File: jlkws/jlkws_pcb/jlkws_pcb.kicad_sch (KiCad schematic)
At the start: 38 parts, among them J0 Conn_01x02_Socket, SW0 SWITCH, SW1 SWITCH, SW10 SWITCH, SW11 SWITCH, SW12 SWITCH, SW13 SWITCH, SW14 SWITCH, SW15 SWITCH, SW16 SWITCH, SW17 SWITCH, SW18 SWITCH, SW19 SWITCH, SW2 SWITCH, SW20 SWITCH, SW21 SWITCH, SW22 SWITCH, SW23 SWITCH, SW24 SWITCH, SW25 SWITCH, SW26 SWITCH, SW27 SWITCH, SW28 SWITCH, SW29 SWITCH, SW3 SWITCH, SW4 SWITCH, SW5 SWITCH, SW6 SWITCH, SW7 SWITCH, SW8 SWITCH, SW9 SWITCH, U0 NICE!

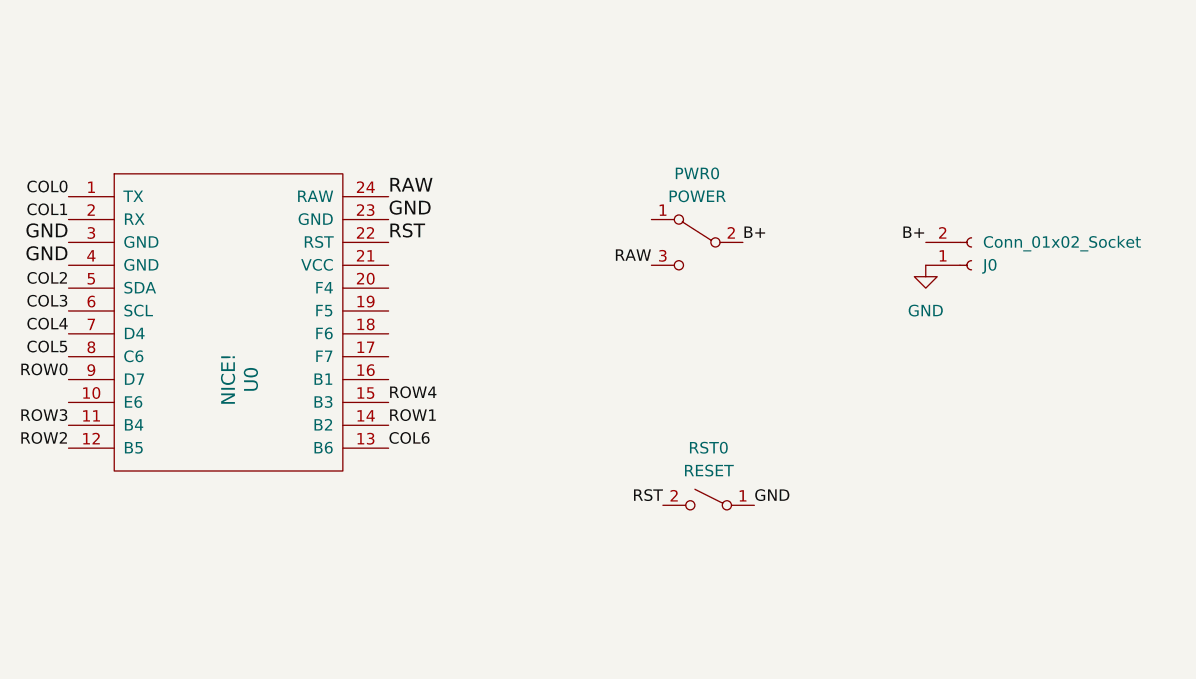
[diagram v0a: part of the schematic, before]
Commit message: Adding jst inter-board connector to jlkws.
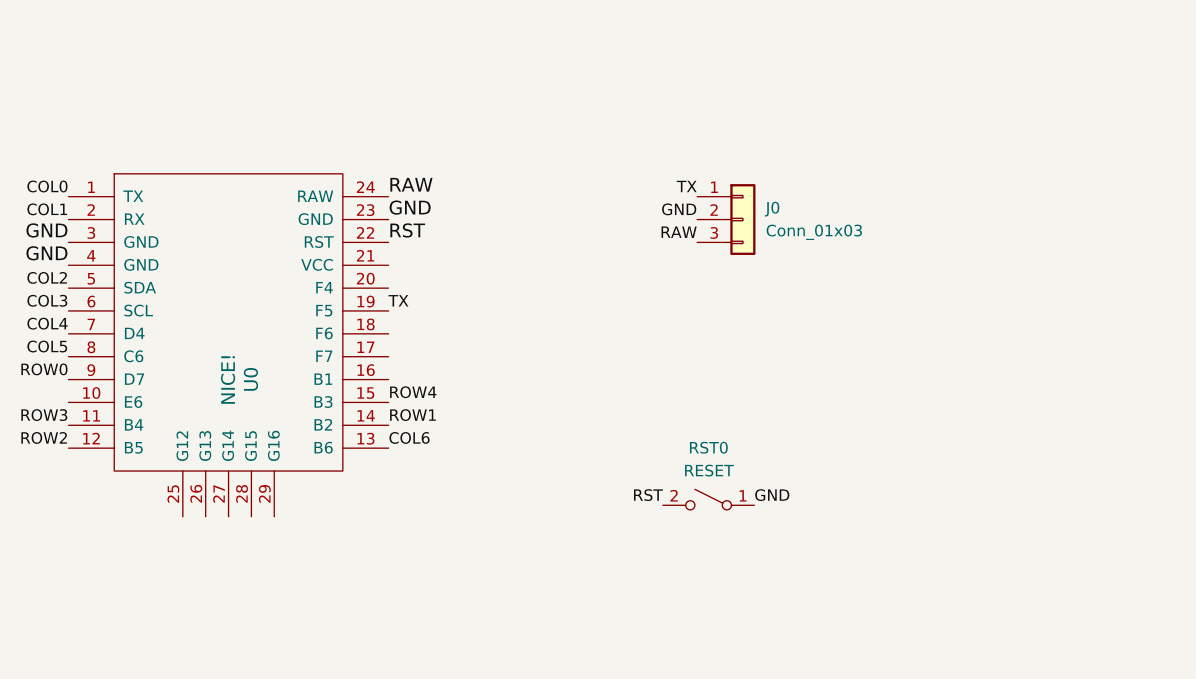
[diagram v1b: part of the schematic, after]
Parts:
- removed J0: Conn_01x02_Socket, Connector_PinHeader_2.54mm:PinHeader_1x02_P2.54mm_Vertical, symbol Connector:Conn_01x02_Socket
- removed PWR0: POWER, footprints:power_switch_1, symbol Switch:SW_SPDT
- added J0: Conn_01x03, Connector_JST:JST_PH_S3B-PH-K_1x03_P2.00mm_Horizontal, symbol Connector_Generic:Conn_01x03
- U0: footprint footprints:nice!nano -> footprints:rp2040_pro_micro
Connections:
- net GND: now also J0.2 (Pin_2)
- net RAW: now also J0.3 (Pin_3)
- net TX: now reaches U0.19 (F5)
- net TX: now also J0.1 (Pin_1)
